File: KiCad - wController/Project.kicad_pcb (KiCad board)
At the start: 2 copper layers, 170.2 x 123.2 mm, 72 parts, among them IC1 ATMEGA328-P, IC2 ATTINY85-P, IC3 ATTINY85-P, M1 Motor, M2 Motor, P1 CONN_02X03, P2 CONN_01X02, P3 CONN_01X02, P4 CONN_01X02, P5 CONN_02X04, P6 CONN_02X03, Q1 Q_NPN_BCE, Q2 Q_NPN_BCE, Q4 Q_NPN_BCE, Q5 NPN, SW4 SW_PUSH, U1 BlueSmirf, U2 LM317, U3 LM317, U6 SN754410NE, Y1 Crystal

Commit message: Started with the PCB
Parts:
- removed P2: CONN_01X02, Pin_Headers:Pin_Header_Straight_1x02
- removed P3, P4: CONN_01X02, Pin_Headers:Pin_Header_Straight_2x01
- removed P5: CONN_02X04, Pin_Headers:Pin_Header_Straight_2x04
- removed P6: CONN_02X03, Pin_Headers:Pin_Header_Straight_2x03
- removed Q1: Q_NPN_BCE, TO_SOT_Packages_THT:TO-92_Inline_Narrow_Oval
- removed R4: 22, Resistors_ThroughHole:Resistor_Vertical_RM5mm
- added DS1: I2C_LCD16X2, Pin_Headers:Pin_Header_Straight_2x03_Pitch2.00mm, F.Cu at (148.5, 105.0)
- added IC4: ATMEGA8-P, Housings_DIP:DIP-28_W7.62mm, F.Cu at (148.5, 105.0)
- added Q3: Q_NPN_BCE, TO_SOT_Packages_THT:TO-92_Inline_Narrow_Oval, F.Cu at (148.5, 105.0)
- added R21: 1K, Resistors_ThroughHole:Resistor_Vertical_RM5mm, F.Cu at (148.5, 105.0)
- added R34, R35, R36: R, Resistors_ThroughHole:Resistor_Vertical_RM5mm, F.Cu at (148.5, 105.0)
- added SW1: Reverse, Wire_Connections_Bridges:WireConnection_1.50mmDrill, F.Cu at (148.5, 105.0)
- added SW2: Start, Wire_Connections_Bridges:WireConnection_1.50mmDrill, F.Cu at (148.5, 105.0)
- added SW3: Lights, Wire_Connections_Bridges:WireConnection_1.50mmDrill, F.Cu at (148.5, 105.0)
- added U5: Linkura, Wire_Connections_Bridges:WireConnection_1.50mmDrill, F.Cu at (148.5, 105.0)
- P1: footprint Pin_Headers:Pin_Header_Straight_2x03 -> Pin_Headers:Pin_Header_Angled_2x03
- R11, R17: value 22 -> 100
- R15, R9: value 100 -> 22
- R19: value 1K -> 22
- U1: footprint Pin_Headers:Pin_Header_Straight_1x06_Pitch2.00mm -> Pin_Headers:Pin_Header_Straight_1x06
- moved R32 83.3 mm to (148.5, 105.0)
- moved R33 79.0 mm to (148.5, 105.0)
- moved Q4 78.7 mm to (148.5, 105.0)
- moved R29 75.0 mm to (148.5, 105.0)
- moved R31 74.0 mm to (148.5, 105.0)
- moved R37 71.7 mm to (148.5, 105.0)
- moved C6 67.9 mm to (148.5, 105.0)
- moved R18 67.1 mm to (148.5, 105.0)
- moved D15 66.9 mm to (148.5, 105.0)
- moved R5 66.3 mm to (148.5, 105.0)
- moved R38 66.2 mm to (148.5, 105.0)
- moved R8 65.9 mm to (148.5, 105.0)
- moved R39 63.3 mm to (148.5, 105.0)
- moved D13 63.2 mm to (148.5, 105.0)
- moved C5 62.4 mm to (148.5, 105.0)
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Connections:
- IC2 pad 7: Net-(IC2-Pad7) -> /IR/SCL
- IC3 pad 1: Net-(IC2-Pad1) -> Net-(IC3-Pad1)
- IC3 pad 7: Net-(IC2-Pad7) -> /IR/SCL
- P1 pad 2: Net-(P1-Pad2) -> /IR/5V
- R11 pad 1: /IR/3V -> /IR/5V
- R11 pad 2: Net-(D6-Pad2) -> /IR/Signal
- R13 pad 2: Net-(D8-Pad2) -> Net-(D6-Pad2)
- R15 pad 1: /IR/5V -> /IR/3V
- R15 pad 2: /IR/Signal -> Net-(D8-Pad2)
- R17 pad 1: /IR/3V -> /IR/5V
- R17 pad 2: Net-(D12-Pad2) -> /IR/Signal
- R19 pad 1: Net-(IC2-Pad1) -> /IR/3V
- R19 pad 2: Net-(Q1-Pad1) -> Net-(D12-Pad2)
- R9 pad 1: /IR/5V -> /IR/3V
- R9 pad 2: /IR/Signal -> Net-(D2-Pad2)
- U1 pad 1: Net-(U1-Pad1) -> (no net)
- U1 pad 2: /IR/5V -> (no net)
- U1 pad 3: GND -> (no net)
- U1 pad 4: Net-(IC1-Pad2) -> (no net)
- U1 pad 5: Net-(IC1-Pad3) -> (no net)
- U1 pad 6: Net-(U1-Pad6) -> (no net)

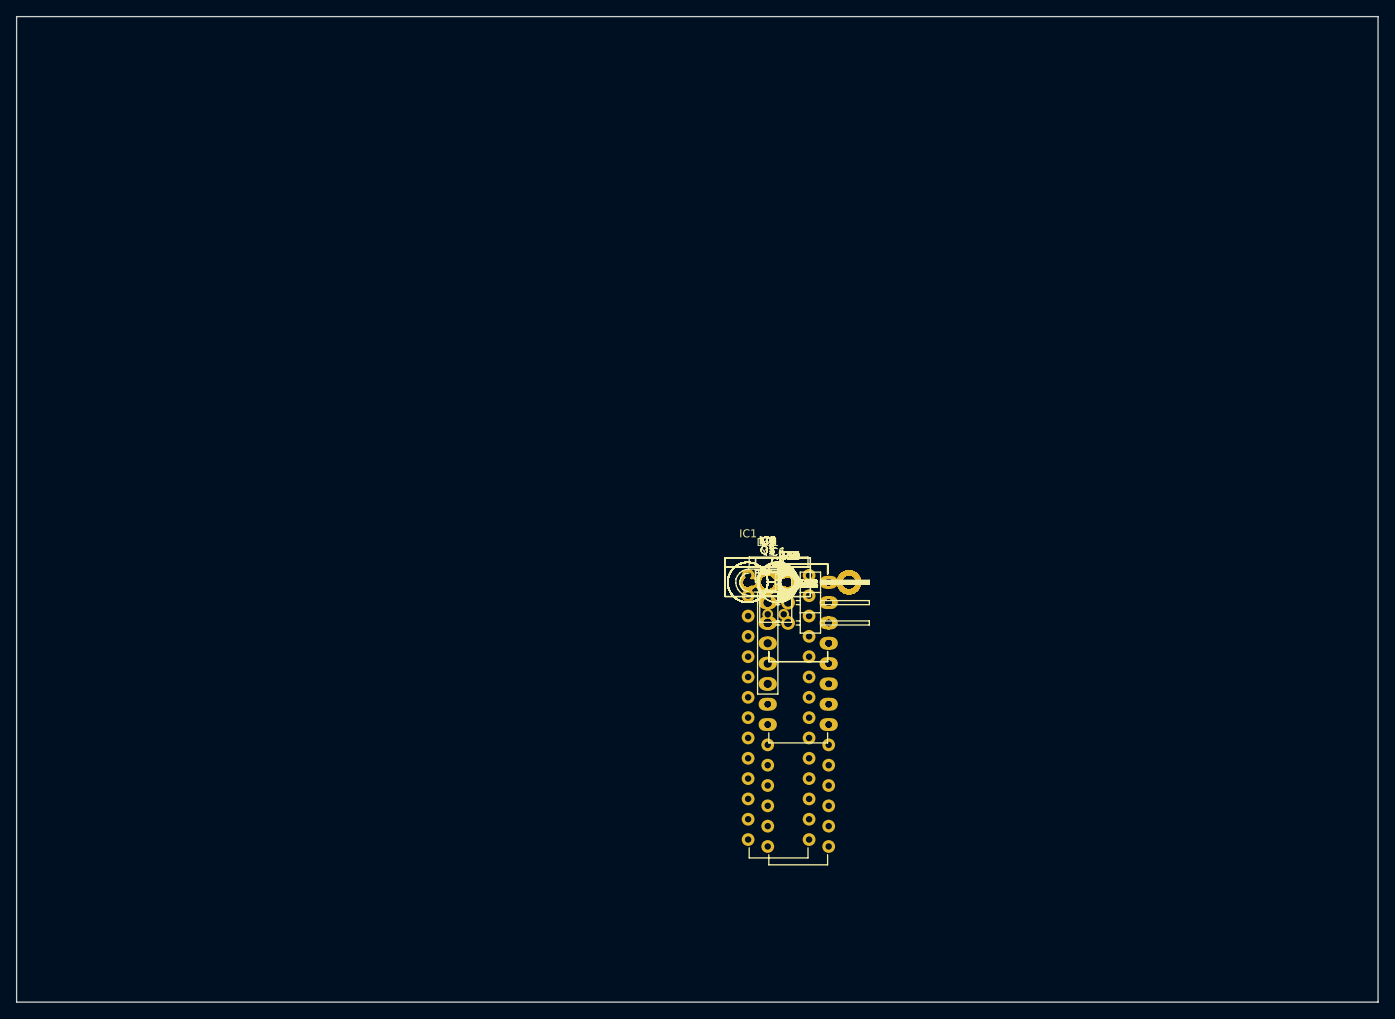
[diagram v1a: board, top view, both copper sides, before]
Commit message: Added code and created PCB for controller
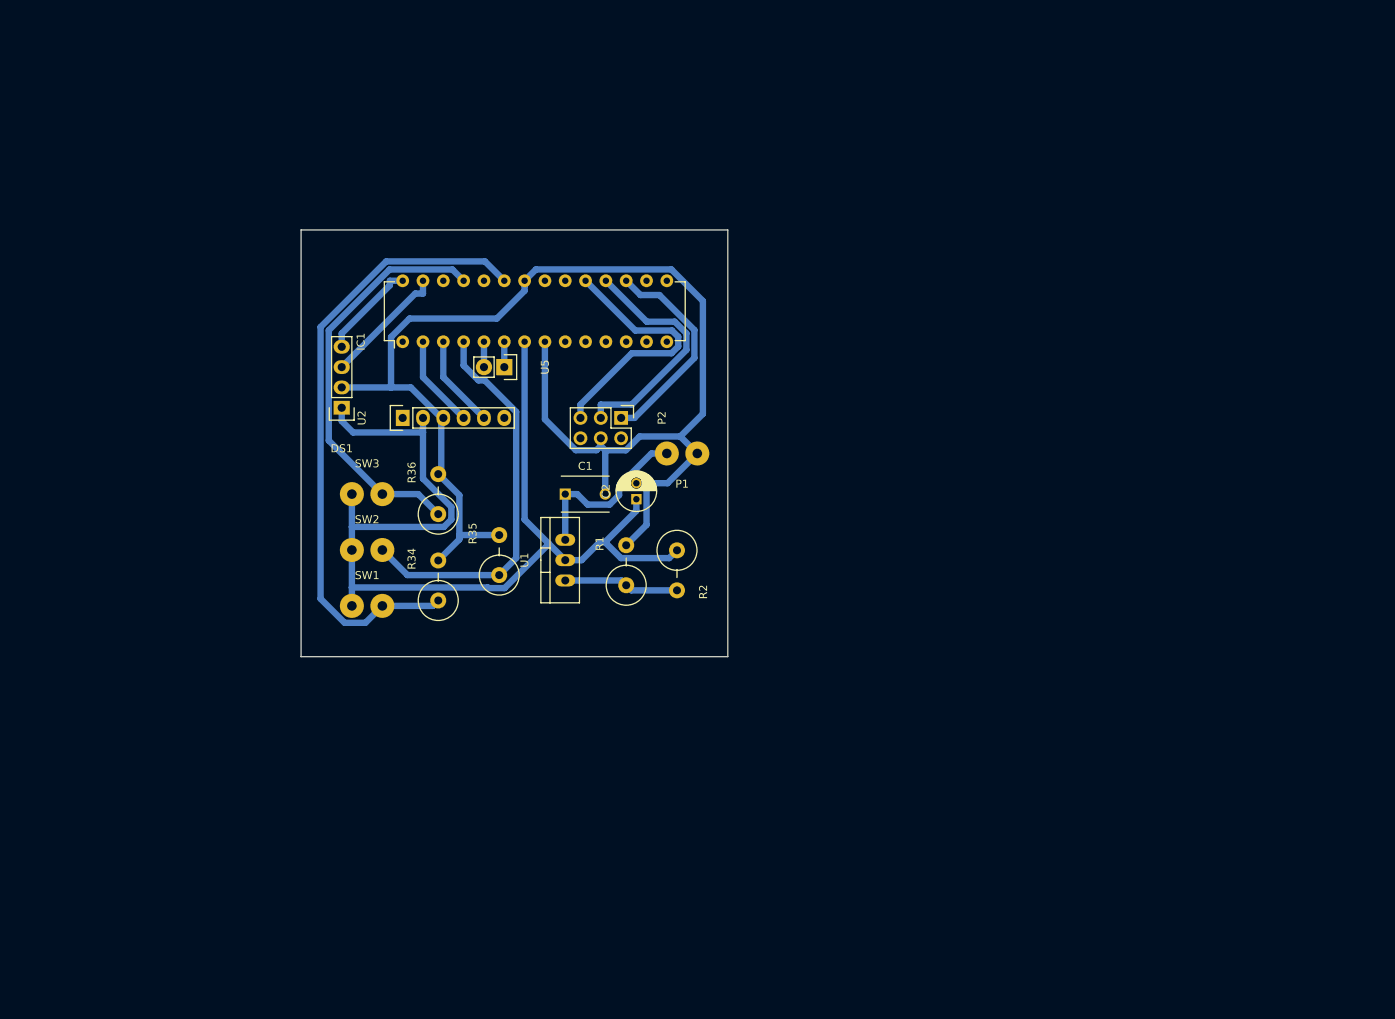
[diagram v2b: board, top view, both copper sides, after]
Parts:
- removed C3, C5: 0.1uF, Capacitors_ThroughHole:C_Disc_D3_P2.5
- removed C4, C6: 1uF, Capacitors_ThroughHole:C_Radial_D5_L6_P2.5
- removed D1, D11, D12, D13, D14, D15, D16, D2, D5, D6, D7, D8: LED, Wire_Connections_Bridges:WireConnection_1.50mmDrill
- removed D10, D3, D4, D9: IR_Recieve, Wire_Connections_Bridges:WireConnection_1.50mmDrill
- removed IC2, IC3: ATTINY85-P, Housings_DIP:DIP-8_W7.62mm
- removed IC4: ATMEGA8-P, Housings_DIP:DIP-28_W7.62mm
- removed M1, M2: Motor, Wire_Connections_Bridges:WireConnection_1.50mmDrill
- removed Q2, Q3, Q4: Q_NPN_BCE, TO_SOT_Packages_THT:TO-92_Inline_Narrow_Oval
- removed Q5: NPN, TO_SOT_Packages_THT:TO-92_Inline_Narrow_Oval
- removed R10, R11, R16, R17: 100, Resistors_ThroughHole:Resistor_Vertical_RM5mm
- removed R12, R13, R14, R15, R18, R19, R31, R37, R8, R9: 22, Resistors_ThroughHole:Resistor_Vertical_RM5mm
- removed R20, R21, R29, R30, R5: 1K, Resistors_ThroughHole:Resistor_Vertical_RM5mm
- removed R22, R6: 330, Resistors_ThroughHole:Resistor_Vertical_RM5mm
- removed R3: Photores, Wire_Connections_Bridges:WireConnection_1.50mmDrill
- removed R32, R33: 10, Resistors_ThroughHole:Resistor_Vertical_RM5mm
- removed R38, R39: 56, Resistors_ThroughHole:Resistor_Vertical_RM5mm
- removed R7: 470, Resistors_ThroughHole:Resistor_Vertical_RM5mm
- removed SW4: SW_PUSH, Wire_Connections_Bridges:WireConnection_1.50mmDrill
- removed U3: LM317, TO_SOT_Packages_THT:TO-220_Neutral123_Vertical
- removed U6: SN754410NE, Housings_DIP:DIP-16_W7.62mm_LongPads
- removed Y1: Crystal, Crystals:Crystal_HC52-U_Vertical
- added P2: SPI, Pin_Headers:Pin_Header_Straight_2x03, F.Cu at (130.2, 84.5)
- C1: value 22pF -> 0.1uF; footprint Capacitors_ThroughHole:C_Disc_D3_P2.5 -> Capacitors_ThroughHole:C_Disc_D6_P5
- C2: value 22pF -> 1uF; footprint Capacitors_ThroughHole:C_Disc_D3_P2.5 -> Capacitors_ThroughHole:C_Radial_D5_L11_P2
- DS1: footprint Pin_Headers:Pin_Header_Straight_2x03_Pitch2.00mm -> Pin_Headers:Pin_Header_Straight_1x04
- IC1: value ATMEGA328-P -> ATMEGA168-P
- P1: value CONN_02X03 -> 9V; footprint Pin_Headers:Pin_Header_Angled_2x03 -> Holes:SolderWirePad1mmmodified
- R2: value 10k -> 330
- R34, R35, R36: value R -> 1k
- SW1, SW3: footprint Wire_Connections_Bridges:WireConnection_1.50mmDrill -> Holes:SolderWirePad1mmmodified
- SW2: value Start -> Pairing; footprint Wire_Connections_Bridges:WireConnection_1.50mmDrill -> Holes:SolderWirePad1mmmodified
- U1: value BlueSmirf -> LM317_SOT223; footprint Pin_Headers:Pin_Header_Straight_1x06 -> TO_SOT_Packages_THT:TO-220_Neutral123_Vertical
- U2: value LM317 -> BlueSmirf; footprint TO_SOT_Packages_THT:TO-220_Neutral123_Vertical -> Pin_Headers:Pin_Header_Straight_1x06
- U5: footprint Wire_Connections_Bridges:WireConnection_1.50mmDrill -> Pin_Headers:Pin_Header_Straight_1x02
- moved DS1 57.5 mm to (95.2, 83.2), turned to 180 degrees
- moved IC1 52.1 mm to (102.9, 74.9), turned to 90 degrees
- moved SW3 51.3 mm to (98.4, 94.0)
- moved SW2 50.2 mm to (98.4, 101.0)
- moved SW1 50.2 mm to (98.4, 108.0)
- moved U2 50.0 mm to (102.9, 84.5), turned to 90 degrees
- moved R36 42.6 mm to (107.3, 94.0), turned to 90 degrees
- moved U5 42.5 mm to (115.6, 78.1), turned to 270 degrees
- moved R34 41.2 mm to (107.3, 104.8), turned to 90 degrees
- moved R35 33.7 mm to (114.9, 101.6), turned to 90 degrees
- moved C1 27.6 mm to (123.2, 94.0)
- moved U1 25.5 mm to (123.2, 102.2), turned to 90 degrees
- moved C2 19.4 mm to (132.1, 94.6), turned to 90 degrees
- moved P1 19.3 mm to (137.8, 88.9), turned to 180 degrees
- moved R1 17.8 mm to (130.8, 102.9), turned to 90 degrees
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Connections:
- C1 pad 1: GND -> Net-(C1-Pad1)
- C1 pad 2: Net-(C1-Pad2) -> GND
- C2 pad 1: GND -> /Controller/5V04
- C2 pad 2: Net-(C2-Pad2) -> GND
- DS1 pad 1: Net-(DS1-Pad1) -> /Controller/5V04
- IC1 pad 10: Net-(C2-Pad2) -> (no net)
- IC1 pad 11: /Motor/Left -> (no net)
- IC1 pad 12: /Motor/Right -> (no net)
- IC1 pad 13: Net-(IC1-Pad13) -> (no net)
- IC1 pad 14: /lights/Brake -> (no net)
- IC1 pad 15: Net-(IC1-Pad15) -> (no net)
- IC1 pad 16: Net-(IC1-Pad16) -> (no net)
- IC1 pad 17: /Motor/Forw. -> Net-(IC1-Pad17)
- IC1 pad 20: Net-(IC1-Pad20) -> (no net)
- IC1 pad 21: Net-(IC1-Pad21) -> (no net)
- IC1 pad 24: Net-(IC1-Pad24) -> (no net)
- IC1 pad 26: /lights/Headlight -> (no net)
- IC1 pad 27: /IR/SDA -> Net-(DS1-Pad3)
- IC1 pad 28: /IR/SCL -> Net-(DS1-Pad4)
- IC1 pad 5: /Motor/Backw. -> Net-(IC1-Pad5)
- IC1 pad 7: /IR/5V -> /Controller/5V04
- IC1 pad 9: Net-(C1-Pad2) -> (no net)
- P1 pad 1: /Motor/Forw. -> GND
- P1 pad 2: /IR/5V -> Net-(C1-Pad1)
- R1 pad 1: GND -> Net-(R1-Pad1)
- R1 pad 2: Net-(IC1-Pad4) -> GND
- R2 pad 1: Net-(IC1-Pad23) -> /Controller/5V04
- R2 pad 2: GND -> Net-(R1-Pad1)
- R34 pad 1: Net-(IC4-Pad14) -> Net-(IC1-Pad23)
- R35 pad 1: Net-(IC4-Pad15) -> Net-(IC1-Pad4)
- R36 pad 1: Net-(IC4-Pad16) -> Net-(IC1-Pad25)
- SW1 pad 1: Net-(DS1-Pad1) -> /Controller/5V04
- SW1 pad 2: Net-(IC4-Pad14) -> Net-(IC1-Pad23)
- SW2 pad 1: Net-(DS1-Pad1) -> /Controller/5V04
- SW2 pad 2: Net-(IC4-Pad15) -> Net-(IC1-Pad4)
- SW3 pad 1: Net-(DS1-Pad1) -> /Controller/5V04
- SW3 pad 2: Net-(IC4-Pad16) -> Net-(IC1-Pad25)
- U1 pad 1: (no net) -> Net-(R1-Pad1)
- U1 pad 2: (no net) -> /Controller/5V04
- U1 pad 3: (no net) -> Net-(C1-Pad1)
- U2 pad 1: Net-(R5-Pad1) -> (no net)
- U2 pad 2: /IR/5V -> /Controller/5V04
- U2 pad 3: +9V -> GND
- U5 pad 1: (no net) -> Net-(IC1-Pad6)
- U5 pad 2: (no net) -> Net-(IC1-Pad5)
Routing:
- net GND: track 0.00 -> 165.5 mm
- net /Controller/5V04: track 0.00 -> 132.9 mm
- net Net-(IC1-Pad23): track 0.00 -> 78.4 mm
- net Net-(IC1-Pad25): track 0.00 -> 51.9 mm
- net Net-(IC1-Pad4): track 0.00 -> 49.1 mm
- net Net-(IC1-Pad19): track 0.00 -> 32.6 mm
- net Net-(IC1-Pad18): track 0.00 -> 30.1 mm
- net Net-(IC1-Pad17): track 0.00 -> 26.8 mm
- net Net-(C1-Pad1): track 0.00 -> 22.3 mm
- net Net-(DS1-Pad3): track 0.00 -> 15.6 mm
- net Net-(R1-Pad1): track 0.00 -> 14.5 mm
- net Net-(DS1-Pad4): track 0.00 -> 12.3 mm
- net Net-(IC1-Pad3): track 0.00 -> 11.6 mm
- net Net-(IC1-Pad2): track 0.00 -> 11.6 mm
- net Net-(IC1-Pad6): track 0.00 -> 3.17 mm
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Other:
- board size 170.2 x 123.2 mm -> 53.3 x 53.3 mm
- net class Default: trace_width 0.25 -> 0.8

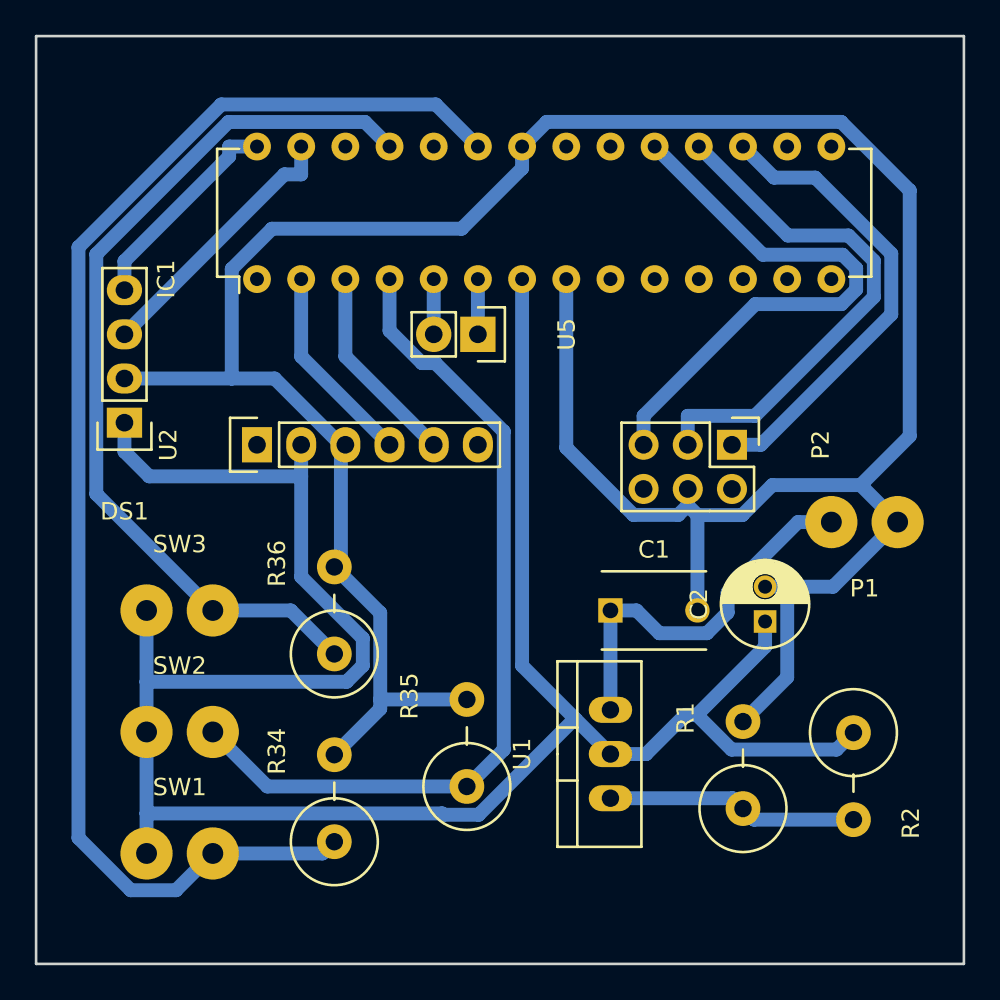
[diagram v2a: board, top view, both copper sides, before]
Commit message: Updated controller PCB and added pariing mode to BT
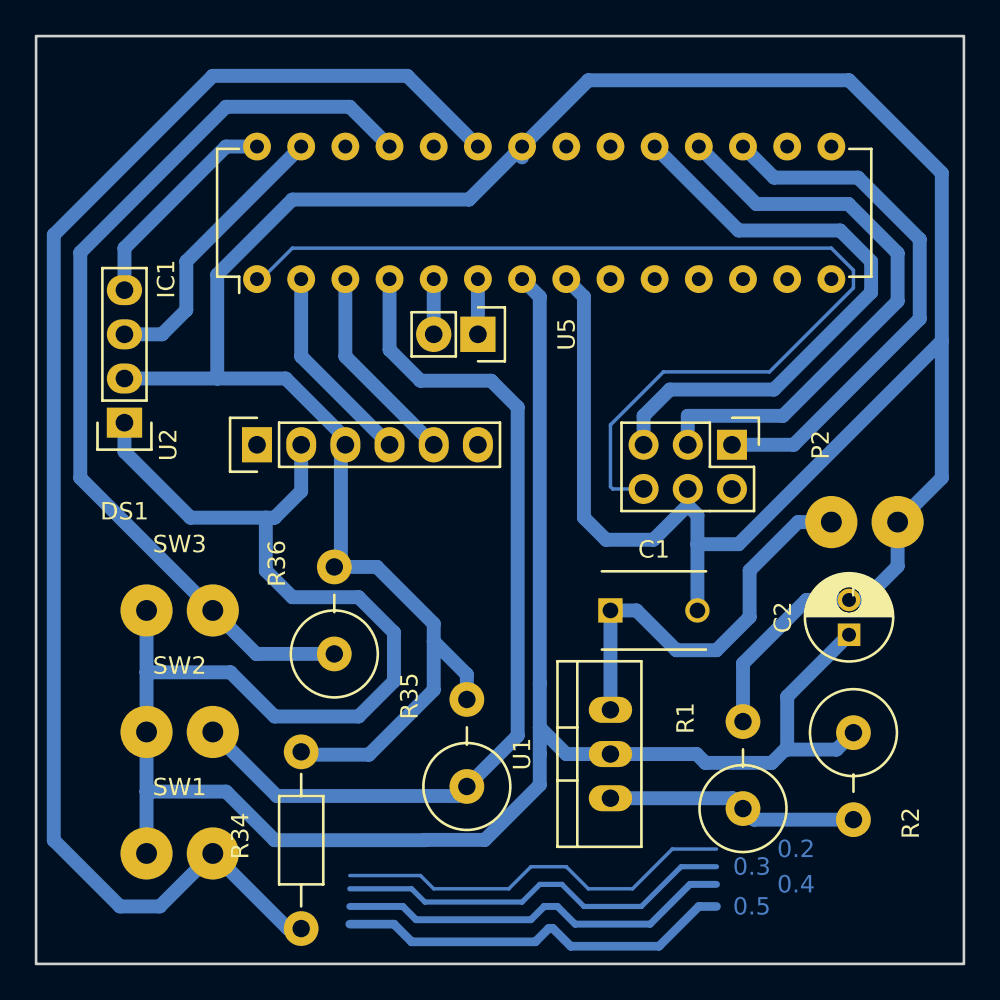
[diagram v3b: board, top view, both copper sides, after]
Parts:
- R34: footprint Resistors_ThroughHole:Resistor_Vertical_RM5mm -> Resistors_ThroughHole:Resistor_Horizontal_RM10mm
- moved R34 7.73 mm to (105.4, 112.3)
- moved C2 4.89 mm to (136.9, 95.4)
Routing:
- net (no net): track 0.00 -> 93.0 mm
- net Net-(IC1-Pad1): track 0.00 -> 59.3 mm
- net GND: track 165.5 -> 187.0 mm
- net /Controller/5V04: track 132.9 -> 144.5 mm
- net Net-(IC1-Pad23): track 78.4 -> 83.5 mm
- net Net-(IC1-Pad17): track 26.8 -> 30.7 mm
- net Net-(IC1-Pad18): track 30.1 -> 33.2 mm
- net Net-(IC1-Pad4): track 49.1 -> 52.2 mm
- net Net-(IC1-Pad25): track 51.9 -> 53.9 mm
- net Net-(IC1-Pad19): track 32.6 -> 34.6 mm
- net Net-(C1-Pad1): track 22.3 -> 24.0 mm
- net Net-(DS1-Pad3): track 15.6 -> 16.3 mm
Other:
- net class Default: via_dia 0.6 -> 0.8
- net class test added: clearance 0.2, trace_width 0.2, via_dia 0.6, via_drill 0.4
- board text added: "0.2"
- board text added: "0.3"
- board text added: "0.4"
- board text added: "0.5"
